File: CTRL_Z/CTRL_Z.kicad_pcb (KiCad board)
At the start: 2 copper layers, 34 x 17 mm, 8 parts, among them J1 BM09B-NSHSS-TBT_LF__SN_

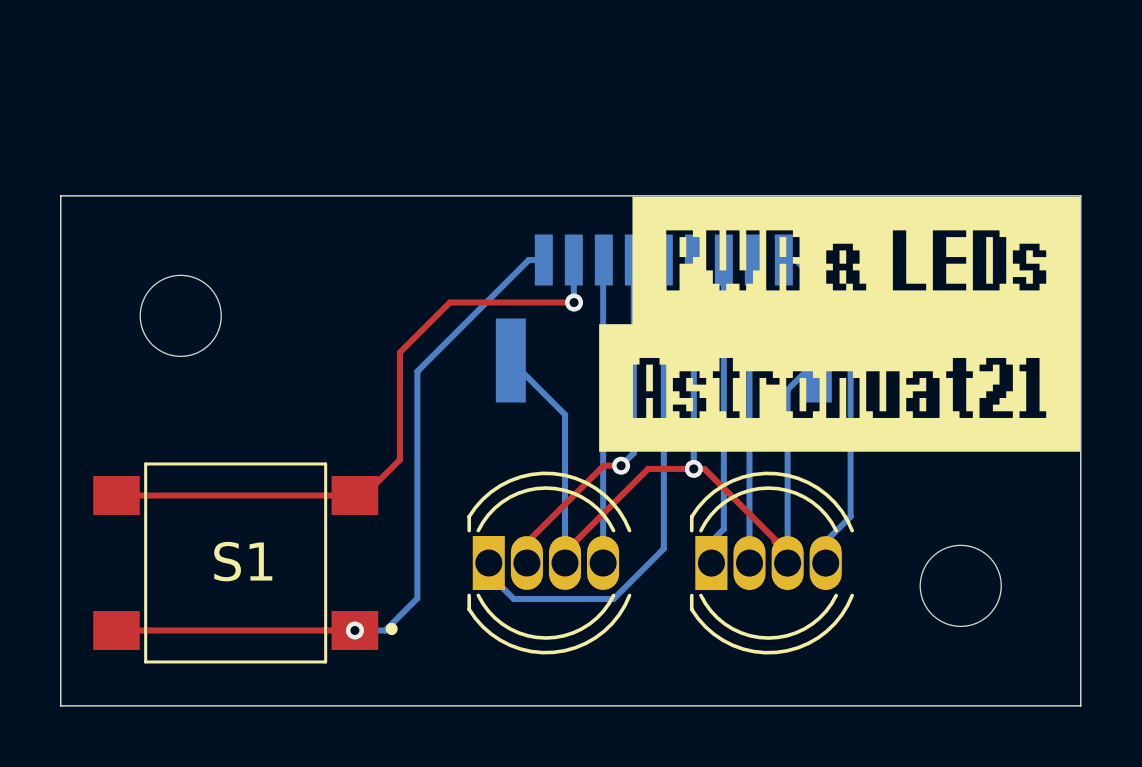
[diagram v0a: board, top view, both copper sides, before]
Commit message: CTRL_Z added, replacement of ZL/ZR
- The X and ZX shoulder buttons now designed in a vertical only layout akin to joysticks.
This removes the need for seperate ZL / ZR PCBs. CTRL_Z as a consequence has differing global labels because of the ambiguity.
This change in design is helpful due to the (5x minimum) nature of ordering PCBs.
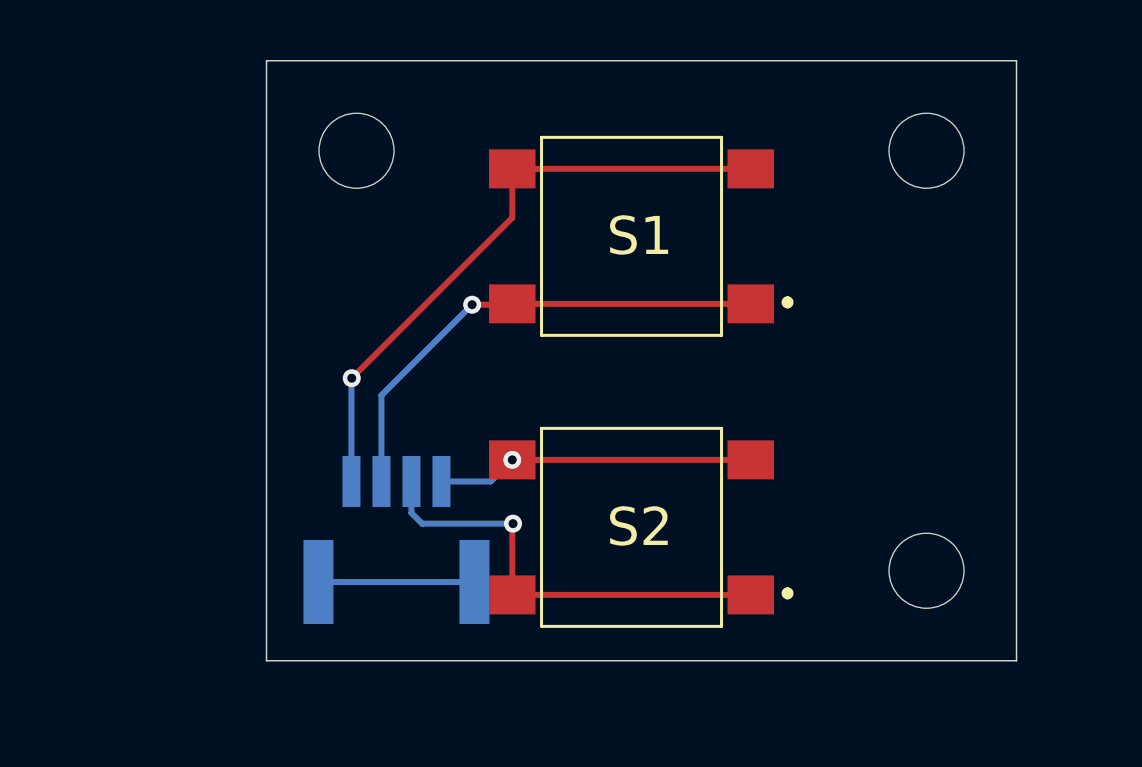
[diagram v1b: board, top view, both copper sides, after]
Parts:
- removed D1: LED_PWR, LED_THT:LED_D5.0mm-4_RGB
- removed D2: LED_WIFI, LED_THT:LED_D5.0mm-4_RGB
- removed kibuzzard-6A2CA9F9: G***, kibuzzard-6A2CA9F9
- removed kibuzzard-6A2CAA19: G***, kibuzzard-6A2CAA19
- added H3: MountingHole, MountingHole:MountingHole_2.5mm, F.Cu at (103.9, 100.5)
- added S2: B3S-1002, B3S-1002:B3S1002, F.Cu at (94.1, 113.0)
- H1, H2: footprint MountingHole:MountingHole_2.7mm_M2.5 -> MountingHole:MountingHole_2.5mm
- J1: value BM09B-NSHSS-TBT_LF__SN_ -> BM04B-NSHSS-TBT_LF__SN_; footprint BM09B-NSHSS-TBT_LF__SN_:BM09BNSHSSTBTLFSN -> BM04B-NSHSS-TBT:BM04BNSHSSTBTLFSN
- moved S1 17.1 mm to (94.1, 103.3)
- moved J1 10.3 mm to (86.3, 113.7)
- moved H1 8.04 mm to (84.9, 100.5)
- moved H2 1.25 mm to (103.9, 114.5)
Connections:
- J1 pad 1: Net-(S1-COM_1) -> ColB
- J1 pad 2: +3V3 -> Row1_X
- J1 pad 3: Net-(D1-RA) -> Row1_ZX
- J1 pad 4: Net-(D1-GA) -> ColA
- J1 pad 5: Net-(D1-BA) -> GND
- S1 pad 1: Net-(S1-COM_1) -> Row1_X
- S1 pad 2: Net-(S1-COM_1) -> Row1_X
- S1 pad 3: +3V3 -> ColB
- S1 pad 4: +3V3 -> ColB
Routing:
- net GND: track 31.1 -> 5.20 mm, vias 1 -> 0
- net Net-(S1-COM_1): track 23.8 -> 0.00 mm, vias 1 -> 0
- net +3V3: track 21.4 -> 0.00 mm, vias 1 -> 0
- net ColB: track 0.00 -> 20.6 mm, vias 0 -> 1
- net Net-(D1-BA): track 16.9 -> 0.00 mm
- net Row1_X: track 0.00 -> 16.4 mm, vias 0 -> 1
- net Row1_ZX: track 0.00 -> 14.9 mm, vias 0 -> 1
- net Net-(D1-GA): track 11.2 -> 0.00 mm, vias 1 -> 0
- net Net-(D2-RA): track 10.9 -> 0.00 mm
- net ColA: track 0.00 -> 10.6 mm, vias 0 -> 1
- net Net-(D2-BA): track 9.56 -> 0.00 mm
- net Net-(D2-GA): track 9.44 -> 0.00 mm
- net Net-(D1-RA): track 9.39 -> 0.00 mm
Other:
- board size 34 x 17 mm -> 25 x 20 mm
